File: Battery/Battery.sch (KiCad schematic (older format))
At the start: 1 part

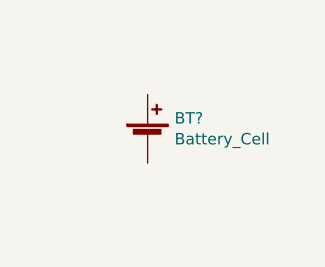
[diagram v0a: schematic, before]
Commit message: Trenin uzdevums pec IV lekcijas
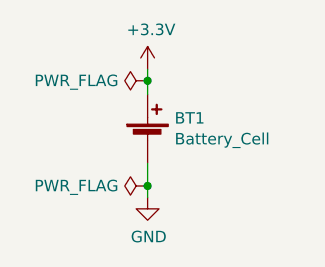
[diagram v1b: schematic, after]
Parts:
- BT1: renamed from BT?; footprint (none) -> Battery_Holder:SMTU2032
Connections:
- net +3V3: now reaches BT1.1 (+)
- net GND: now reaches BT1.2 (-)
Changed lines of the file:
@@
 $EndDescr
 $Comp
-L Device:Battery_Cell BT?
+L Device:Battery_Cell BT1
 U 1 1 5FBD8D1E
 P 5850 3890
-F 0 "BT?" H 5968 3986 50  0000 L CNN
+F 0 "BT1" H 5968 3986 50  0000 L CNN
 F 1 "Battery_Cell" H 5968 3895 50  0000 L CNN
-F 2 "" V 5850 3950 50  0001 C CNN
+F 2 "Battery_Holder:SMTU2032" V 5850 3950 50  0001 C CNN
 F 3 "~" V 5850 3950 50  0001 C CNN
 	1    5850 3890
 	1    0    0    -1
 $EndComp
+$Comp
+L power:+3.3V #PWR01
+U 1 1 5FBD917C
+P 5850 3580
+F 0 "#PWR01" H 5850 3430 50  0001 C CNN
+F 1 "+3.3V" H 5865 3753 50  0000 C CNN
+F 2 "" H 5850 3580 50  0001 C CNN
+F 3 "" H 5850 3580 50  0001 C CNN
+	1    5850 3580
+	1    0    0    -1
+$EndComp
+Wire Wire Line
+	5850 3580 5850 3630
+$Comp
+L power:GND #PWR02
+U 1 1 5FBD9D34
+P 5850 4140
+F 0 "#PWR02" H 5850 3890 50  0001 C CNN
+F 1 "GND" H 5855 3967 50  0000 C CNN
+F 2 "" H 5850 4140 50  0001 C CNN
+F 3 "" H 5850 4140 50  0001 C CNN
+	1    5850 4140
+	1    0    0    -1
+$EndComp
+Wire Wire Line
+	5850 3990 5850 4090
+$Comp
+L power:PWR_FLAG #FLG0101
+U 1 1 5FBDA4E7
+P 5850 3630
+F 0 "#FLG0101" H 5850 3705 50  0001 C CNN
+F 1 "PWR_FLAG" V 5850 3757 50  0000 L CNN
+F 2 "" H 5850 3630 50  0001 C CNN
+F 3 "~" H 5850 3630 50  0001 C CNN
+	1    5850 3630
+	0    -1   -1   0
+$EndComp
+Connection ~ 5850 3630
+Wire Wire Line
+	5850 3630 5850 3690
+$Comp
+L power:PWR_FLAG #FLG0102
+U 1 1 5FBDAE4B
+P 5850 4090
+F 0 "#FLG0102" H 5850 4165 50  0001 C CNN
+F 1 "PWR_FLAG" V 5850 4217 50  0000 L CNN
+F 2 "" H 5850 4090 50  0001 C CNN
+F 3 "~" H 5850 4090 50  0001 C CNN
+	1    5850 4090
+	0    -1   -1   0
+$EndComp
+Connection ~ 5850 4090
+Wire Wire Line
+	5850 4090 5850 4140
 $EndSCHEMATC

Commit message: Battery holders HW
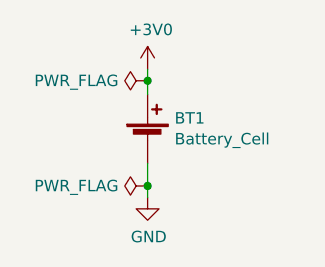
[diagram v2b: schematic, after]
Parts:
- BT1: footprint Battery_Holder:SMTU2032 -> Battery_Holder:12BH062-GR
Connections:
- net +3V3 renamed +3V0
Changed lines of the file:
@@
 F 0 "BT1" H 5968 3986 50  0000 L CNN
 F 1 "Battery_Cell" H 5968 3895 50  0000 L CNN
-F 2 "Battery_Holder:SMTU2032" V 5850 3950 50  0001 C CNN
+F 2 "Battery_Holder:12BH062-GR" V 5850 3950 50  0001 C CNN
 F 3 "~" V 5850 3950 50  0001 C CNN
 	1    5850 3890
-	1    0    0    -1
-$EndComp
-$Comp
-L power:+3.3V #PWR01
-U 1 1 5FBD917C
-P 5850 3580
-F 0 "#PWR01" H 5850 3430 50  0001 C CNN
-F 1 "+3.3V" H 5865 3753 50  0000 C CNN
-F 2 "" H 5850 3580 50  0001 C CNN
-F 3 "" H 5850 3580 50  0001 C CNN
-	1    5850 3580
 	1    0    0    -1
 $EndComp
@@
 Wire Wire Line
 	5850 4090 5850 4140
+$Comp
+L power:+3V0 #PWR0101
+U 1 1 5FBD9DFC
+P 5850 3580
+F 0 "#PWR0101" H 5850 3430 50  0001 C CNN
+F 1 "+3V0" H 5865 3753 50  0000 C CNN
+F 2 "" H 5850 3580 50  0001 C CNN
+F 3 "" H 5850 3580 50  0001 C CNN
+	1    5850 3580
+	1    0    0    -1
+$EndComp
 $EndSCHEMATC
